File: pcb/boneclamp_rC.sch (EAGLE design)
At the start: 135 parts, among them U1 OPA365AIDBVR, U10 AD5686, U11 LM2663, U12 MAX1735, U13 TLV70245, U14 REF5040, U15 AD8032, U16 24C, U2 OPA365AIDBVR, U3 OPA365AIDBVR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

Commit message: More routing.
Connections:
- removed net N$17: C31.2, R28.1
- net AGND: now also C31.2, R28.1
- net VDD_5V: no longer BB1.VDD_5V@1
- net VDRIVE: no longer BB1.VDD_3V3EXP@1
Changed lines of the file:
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@@
 <part name="SUPPLY14" library="supply2" deviceset="AGND" device=""/>
 <part name="SUPPLY15" library="supply2" deviceset="AGND" device=""/>
-<part name="SUPPLY16" library="supply2" deviceset="AGND" device=""/>
 <part name="DAC_D+" library="testpad" deviceset="TP" device="B1,27"/>
 <part name="DAC_C+" library="testpad" deviceset="TP" device="B1,27"/>
@@
 <part name="C46" library="rcl" deviceset="C-EU" device="C0603" value="1uF"/>
 <part name="SUPPLY38" library="supply2" deviceset="AGND" device=""/>
+<part name="SUPPLY16" library="supply2" deviceset="AGND" device=""/>
 </parts>
 <sheets>
@@
 <net name="VDRIVE" class="0">
 <segment>
-<pinref part="BB1" gate="G$1" pin="VDD_3V3EXP@1"/>
-<wire x1="-63.5" y1="40.64" x2="-81.28" y2="40.64" width="0.1524" layer="91"/>
-<label x="-81.28" y="40.64" size="1.778" layer="95"/>
-</segment>
-<segment>
 <pinref part="BB1" gate="G$1" pin="VDD_3V3EXP@2"/>
 <wire x1="-7.62" y1="40.64" x2="10.16" y2="40.64" width="0.1524" layer="91"/>
@@
 </net>
 <net name="VDD_5V" class="0">
-<segment>
-<pinref part="BB1" gate="G$1" pin="VDD_5V@1"/>
-<wire x1="-63.5" y1="38.1" x2="-81.28" y2="38.1" width="0.1524" layer="91"/>
-<label x="-81.28" y="38.1" size="1.778" layer="95"/>
-</segment>
 <segment>
 <pinref part="BB1" gate="G$1" pin="VDD_5V@2"/>
@@
 <instance part="SUPPLY14" gate="G$1" x="48.26" y="-45.72"/>
 <instance part="SUPPLY15" gate="G$1" x="48.26" y="-68.58"/>
-<instance part="SUPPLY16" gate="G$1" x="48.26" y="-90.805"/>
 <instance part="DAC_D+" gate="G$1" x="35.56" y="-5.08"/>
 <instance part="DAC_C+" gate="G$1" x="35.56" y="-27.94"/>
@@
 <instance part="C22" gate="G$1" x="106.68" y="60.96"/>
 <instance part="SUPPLY21" gate="G$1" x="114.3" y="43.18"/>
+<instance part="SUPPLY16" gate="G$1" x="48.26" y="-91.44"/>
 </instances>
 <busses>
@@
 <junction x="106.68" y="81.28"/>
 <label x="99.06" y="81.28" size="1.778" layer="95"/>
-</segment>
-</net>
-<net name="N$17" class="0">
-<segment>
-<pinref part="R28" gate="G$1" pin="1"/>
-<wire x1="43.18" y1="-88.9" x2="48.26" y2="-88.9" width="0.1524" layer="91"/>
-<pinref part="C31" gate="G$1" pin="2"/>
-<wire x1="48.26" y1="-88.9" x2="53.34" y2="-88.9" width="0.1524" layer="91"/>
-<wire x1="53.34" y1="-88.9" x2="53.34" y2="-86.36" width="0.1524" layer="91"/>
-<wire x1="48.26" y1="-88.9" x2="48.26" y2="-91.44" width="0.1524" layer="91"/>
-<junction x="48.26" y="-88.9"/>
 </segment>
 </net>
@@
 <pinref part="SUPPLY21" gate="G$1" pin="AGND"/>
 </segment>
-</net>
+<segment>
+<pinref part="R28" gate="G$1" pin="1"/>
+<pinref part="C31" gate="G$1" pin="2"/>
+<wire x1="43.18" y1="-88.9" x2="48.26" y2="-88.9" width="0.1524" layer="91"/>
+<wire x1="48.26" y1="-88.9" x2="53.34" y2="-88.9" width="0.1524" layer="91"/>
+<wire x1="53.34" y1="-88.9" x2="53.34" y2="-86.36" width="0.1524" layer="91"/>
+<pinref part="SUPPLY16" gate="G$1" pin="AGND"/>
+<junction x="48.26" y="-88.9"/>
+</segment>
+</net>

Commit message: Routing almost complete.
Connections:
- net AGND: no longer U10.GAIN, U10.GND, U10.RSTSEL, U10.SDO
- net DGND: now also U10.GAIN, U10.GND, U10.RSTSEL, U10.SDO

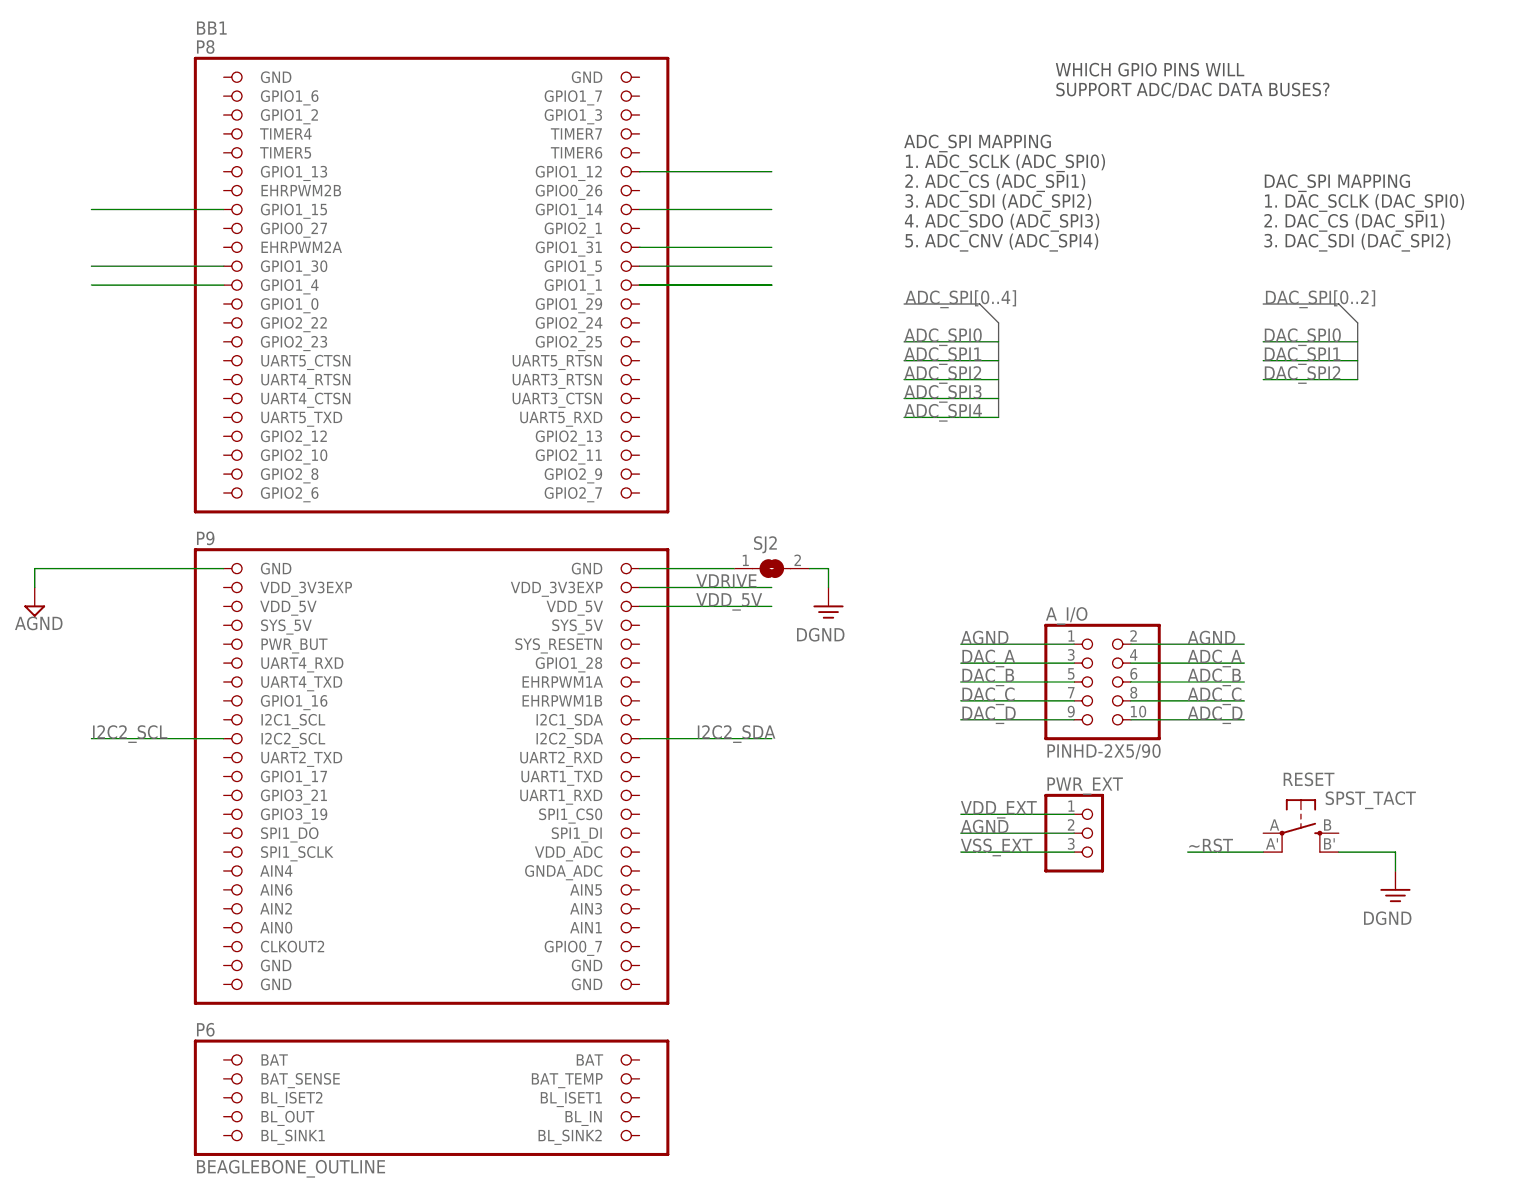
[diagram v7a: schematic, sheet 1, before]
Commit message: Finished first intetation of routing! Need to clean up the silkscreen, check for single ended wires, double check schematic wiring, run DRC, and send it to fab.
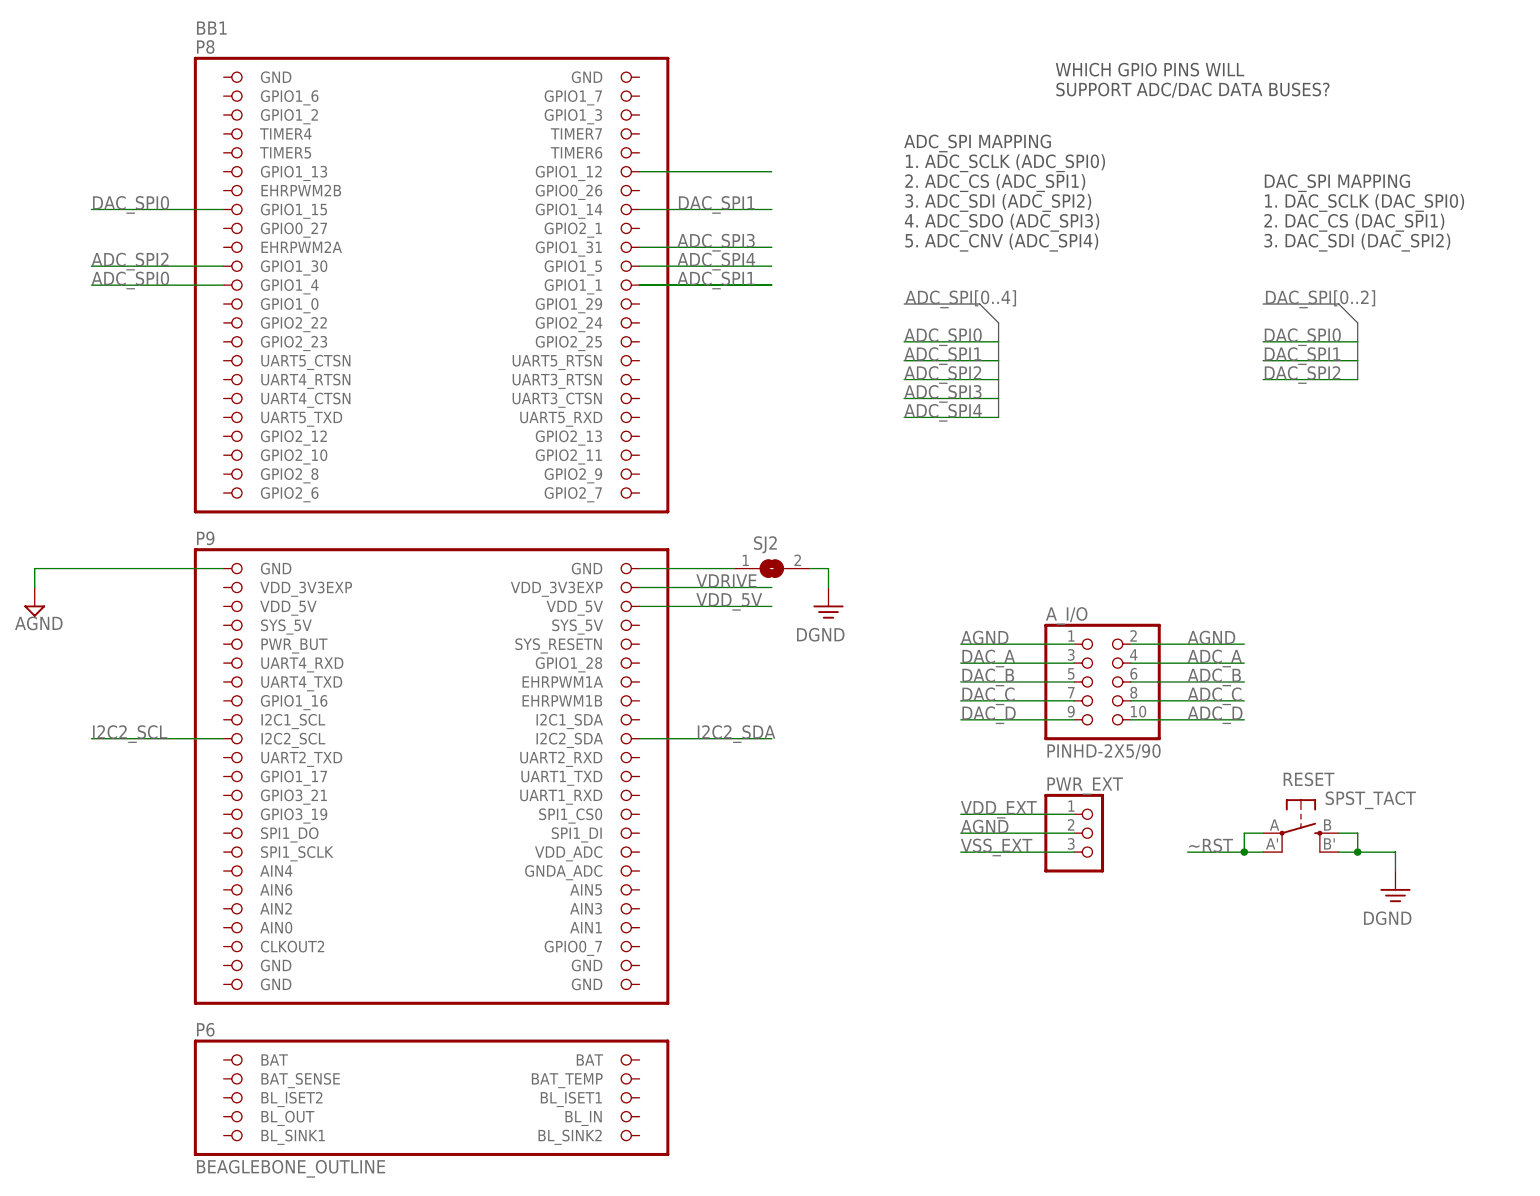
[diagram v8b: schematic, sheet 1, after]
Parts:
- +4.5V, VDRIVE: value TPB1,27 -> TPPAD1-17; device testpad:TPB1,27 -> testpad:TPPAD1-17
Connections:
- new net N$16: C15.2, R14.1, U5.REF+
- net AGND: now also U10.GND
- net DGND: now also RESET.S; no longer U10.GND, U10.SDO
- net VREF: no longer C15.2, R14.1, U5.REF+
- net ~RST: now also RESET.P
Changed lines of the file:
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@@
 <part name="U10" library="analog-devices-02" deviceset="AD5686RARUZ" device="" value="AD5686"/>
 <part name="I2C2_SCLK" library="testpad" deviceset="TP" device="B1,27"/>
-<part name="VDRIVE" library="testpad" deviceset="TP" device="B1,27"/>
+<part name="VDRIVE" library="testpad" deviceset="TP" device="PAD1-17" value="TPPAD1-17"/>
 <part name="U13" library="ti-extended" deviceset="TLV70025DDCR" device="" value="TLV70245"/>
 <part name="C36" library="rcl" deviceset="C-EU" device="C0603" value="1uF"/>
@@
 <part name="R29" library="rcl" deviceset="R-US_" device="R0603" value="10k"/>
 <part name="-4.5V" library="testpad" deviceset="TP" device="B1,27"/>
-<part name="+4.5V" library="testpad" deviceset="TP" device="B1,27"/>
+<part name="+4.5V" library="testpad" deviceset="TP" device="PAD1-17" value="TPPAD1-17"/>
 <part name="VSS_PRE" library="testpad" deviceset="TP" device="B1,27"/>
 <part name="DGND6" library="supply2" deviceset="PE" device="" value="DGND"/>
@@
 <part name="SUPPLY16" library="supply2" deviceset="AGND" device=""/>
 <part name="DGND9" library="supply2" deviceset="PE" device="" value="DGND"/>
+<part name="SUPPLY2" library="supply2" deviceset="AGND" device=""/>
 </parts>
 <sheets>
@@
 <segment>
 <pinref part="RESET" gate="G$1" pin="S1"/>
-<wire x1="86.36" y1="5.08" x2="93.98" y2="5.08" width="0.1524" layer="91"/>
+<wire x1="86.36" y1="5.08" x2="88.9" y2="5.08" width="0.1524" layer="91"/>
 <pinref part="DGND10" gate="PE" pin="PE"/>
+<wire x1="88.9" y1="5.08" x2="93.98" y2="5.08" width="0.1524" layer="91"/>
 <wire x1="93.98" y1="2.54" x2="93.98" y2="5.08" width="0.1524" layer="91"/>
+<pinref part="RESET" gate="G$1" pin="S"/>
+<wire x1="86.36" y1="7.62" x2="88.9" y2="7.62" width="0.1524" layer="91"/>
+<wire x1="88.9" y1="7.62" x2="88.9" y2="5.08" width="0.1524" layer="91"/>
+<junction x="88.9" y="5.08"/>
 </segment>
 <segment>
@@
 <pinref part="BB1" gate="G$1" pin="GPIO1_4"/>
 <wire x1="-63.5" y1="81.28" x2="-81.28" y2="81.28" width="0.1524" layer="91"/>
+<label x="-81.28" y="81.28" size="1.778" layer="95"/>
 </segment>
 </net>
@@
 <wire x1="-7.62" y1="81.28" x2="10.16" y2="81.28" width="0.1524" layer="91"/>
 <wire x1="-7.62" y1="81.28" x2="10.16" y2="81.28" width="0.1524" layer="91"/>
+<label x="-2.54" y="81.28" size="1.778" layer="95"/>
 </segment>
 </net>
@@
 <pinref part="BB1" gate="G$1" pin="GPIO1_30"/>
 <wire x1="-63.5" y1="83.82" x2="-81.28" y2="83.82" width="0.1524" layer="91"/>
+<label x="-81.28" y="83.82" size="1.778" layer="95"/>
 </segment>
 </net>
@@
 <pinref part="BB1" gate="G$1" pin="GPIO1_31"/>
 <wire x1="-7.62" y1="86.36" x2="10.16" y2="86.36" width="0.1524" layer="91"/>
+<label x="-2.54" y="86.36" size="1.778" layer="95"/>
 </segment>
 </net>
@@
 <pinref part="BB1" gate="G$1" pin="GPIO1_5"/>
 <wire x1="-7.62" y1="83.82" x2="10.16" y2="83.82" width="0.1524" layer="91"/>
+<label x="-2.54" y="83.82" size="1.778" layer="95"/>
 </segment>
 </net>
@@
 <pinref part="BB1" gate="G$1" pin="GPIO1_15"/>
 <wire x1="-63.5" y1="91.44" x2="-81.28" y2="91.44" width="0.1524" layer="91"/>
+<label x="-81.28" y="91.44" size="1.778" layer="95"/>
 </segment>
 </net>
@@
 <pinref part="BB1" gate="G$1" pin="GPIO1_14"/>
 <wire x1="-7.62" y1="91.44" x2="10.16" y2="91.44" width="0.1524" layer="91"/>
+<label x="-2.54" y="91.44" size="1.778" layer="95"/>
 </segment>
 </net>
@@
 <segment>
 <pinref part="RESET" gate="G$1" pin="P1"/>
-<wire x1="76.2" y1="5.08" x2="66.04" y2="5.08" width="0.1524" layer="91"/>
+<wire x1="76.2" y1="5.08" x2="73.66" y2="5.08" width="0.1524" layer="91"/>
 <label x="66.04" y="5.08" size="1.778" layer="95"/>
+<pinref part="RESET" gate="G$1" pin="P"/>
+<wire x1="73.66" y1="5.08" x2="66.04" y2="5.08" width="0.1524" layer="91"/>
+<wire x1="76.2" y1="7.62" x2="73.66" y2="7.62" width="0.1524" layer="91"/>
+<wire x1="73.66" y1="7.62" x2="73.66" y2="5.08" width="0.1524" layer="91"/>
+<junction x="73.66" y="5.08"/>
 </segment>
 </net>
@@
 <net name="VREF" class="0">
 <segment>
-<pinref part="U5" gate="A" pin="REF+"/>
-<wire x1="50.8" y1="55.88" x2="38.1" y2="55.88" width="0.1524" layer="91"/>
-<pinref part="C15" gate="G$1" pin="2"/>
-<wire x1="38.1" y1="53.34" x2="38.1" y2="55.88" width="0.1524" layer="91"/>
-<pinref part="R14" gate="G$1" pin="1"/>
-<wire x1="22.86" y1="55.88" x2="38.1" y2="55.88" width="0.1524" layer="91"/>
-<junction x="38.1" y="55.88"/>
-</segment>
-<segment>
 <pinref part="R14" gate="G$1" pin="2"/>
 <wire x1="12.7" y1="55.88" x2="2.54" y2="55.88" width="0.1524" layer="91"/>
@@
 <wire x1="45.72" y1="91.44" x2="45.72" y2="76.2" width="0.1524" layer="91"/>
 <wire x1="45.72" y1="76.2" x2="50.8" y2="76.2" width="0.1524" layer="91"/>
+</segment>
+</net>
+<net name="N$16" class="0">
+<segment>
+<pinref part="R14" gate="G$1" pin="1"/>
+<pinref part="U5" gate="A" pin="REF+"/>
+<wire x1="22.86" y1="55.88" x2="38.1" y2="55.88" width="0.1524" layer="91"/>
+<pinref part="C15" gate="G$1" pin="2"/>
+<wire x1="38.1" y1="55.88" x2="50.8" y2="55.88" width="0.1524" layer="91"/>
+<wire x1="38.1" y1="53.34" x2="38.1" y2="55.88" width="0.1524" layer="91"/>
+<junction x="38.1" y="55.88"/>
 </segment>
 </net>
@@
 <instance part="SUPPLY16" gate="G$1" x="48.26" y="-91.44"/>
 <instance part="DGND9" gate="PE" x="-33.02" y="-30.48"/>
+<instance part="SUPPLY2" gate="G$1" x="-20.32" y="-22.86"/>
 </instances>
 <busses>
@@
 <pinref part="SUPPLY16" gate="G$1" pin="AGND"/>
 <junction x="48.26" y="-88.9"/>
+</segment>
+<segment>
+<pinref part="SUPPLY2" gate="G$1" pin="AGND"/>
+<wire x1="-20.32" y1="-20.32" x2="-20.32" y2="-15.24" width="0.1524" layer="91"/>
+<pinref part="U10" gate="G$1" pin="GND"/>
+<wire x1="-20.32" y1="-15.24" x2="-17.78" y2="-15.24" width="0.1524" layer="91"/>
 </segment>
 </net>
@@
 </segment>
 <segment>
-<wire x1="-33.02" y1="-27.94" x2="-33.02" y2="-15.24" width="0.1524" layer="91"/>
-<pinref part="U10" gate="G$1" pin="GND"/>
-<wire x1="-33.02" y1="-15.24" x2="-17.78" y2="-15.24" width="0.1524" layer="91"/>
-<junction x="-33.02" y="-15.24"/>
+<wire x1="-33.02" y1="-27.94" x2="-33.02" y2="-5.08" width="0.1524" layer="91"/>
 <pinref part="U10" gate="G$1" pin="RSTSEL"/>
 <wire x1="-17.78" y1="5.08" x2="-33.02" y2="5.08" width="0.1524" layer="91"/>
 <wire x1="-33.02" y1="5.08" x2="-33.02" y2="-5.08" width="0.1524" layer="91"/>
 <pinref part="U10" gate="G$1" pin="GAIN"/>
-<wire x1="-33.02" y1="-5.08" x2="-33.02" y2="-15.24" width="0.1524" layer="91"/>
 <wire x1="-33.02" y1="-5.08" x2="-17.78" y2="-5.08" width="0.1524" layer="91"/>
 <junction x="-33.02" y="-5.08"/>
-<wire x1="-33.02" y1="5.08" x2="-33.02" y2="12.7" width="0.1524" layer="91"/>
-<junction x="-33.02" y="5.08"/>
-<pinref part="U10" gate="G$1" pin="SDO"/>
-<wire x1="-33.02" y1="12.7" x2="-17.78" y2="12.7" width="0.1524" layer="91"/>
 <pinref part="DGND9" gate="PE" pin="PE"/>
 </segment>
